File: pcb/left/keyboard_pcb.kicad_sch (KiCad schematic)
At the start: 33 parts, among them J1 TRRS, K00 KEYSW, K01 KEYSW, K02 KEYSW, K03 KEYSW, K04 KEYSW, K05 KEYSW, K10 KEYSW, K11 KEYSW, K12 KEYSW, K13 KEYSW, K14 KEYSW, K15 KEYSW, K20 KEYSW, K21 KEYSW, K22 KEYSW, K23 KEYSW, K24 KEYSW, K25 KEYSW, K30 KEYSW, K31 KEYSW, K32 KEYSW, U2 Pico

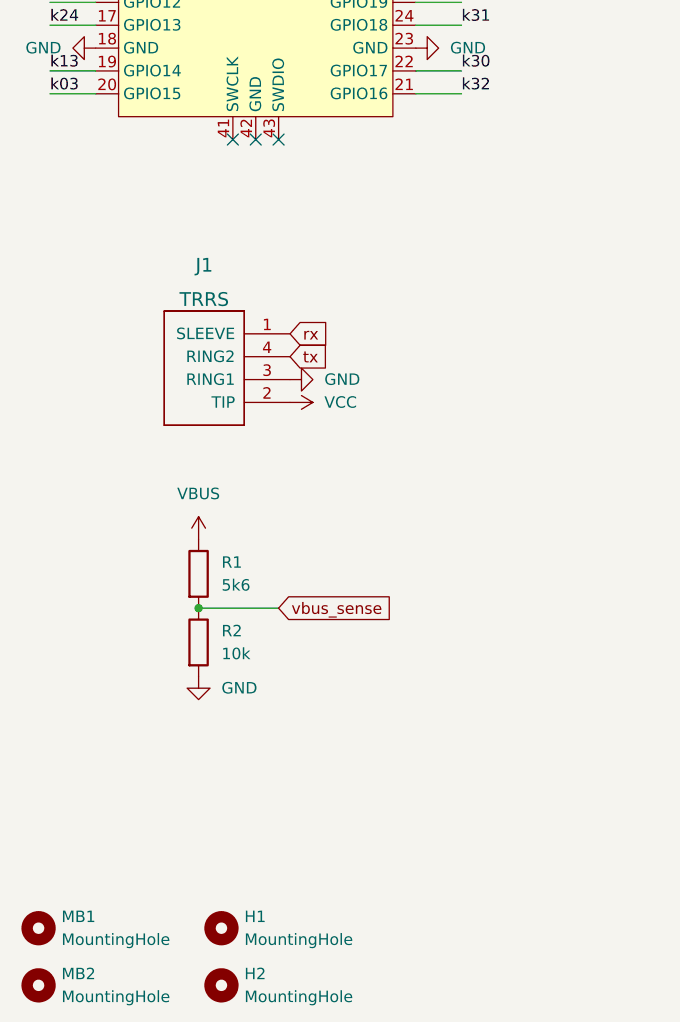
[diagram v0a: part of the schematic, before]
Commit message: Replace TRRS with USB-C on left side
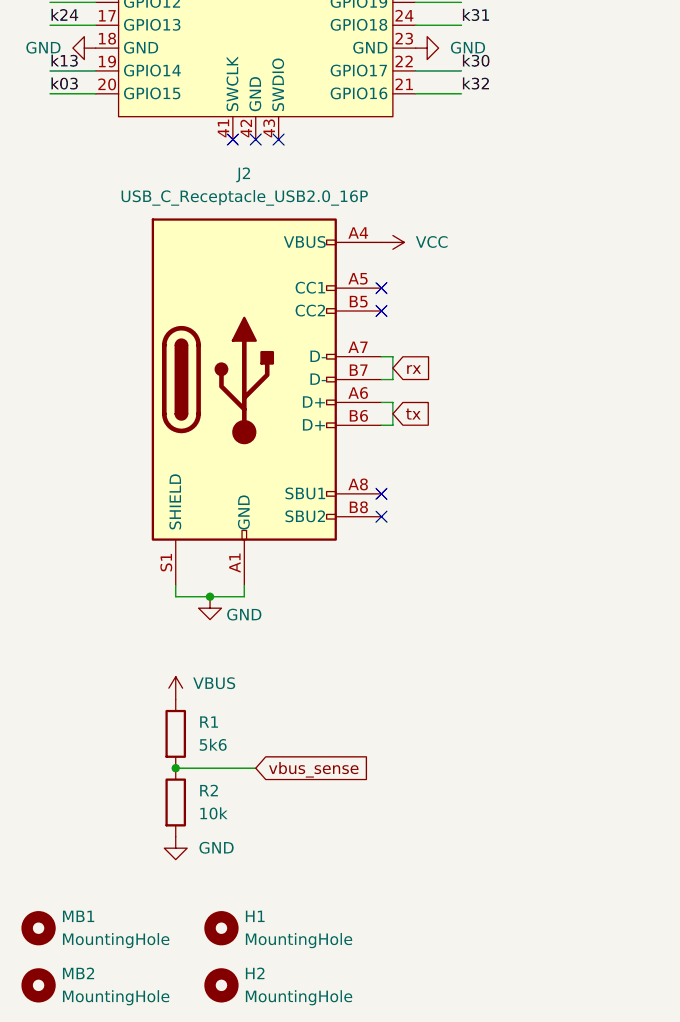
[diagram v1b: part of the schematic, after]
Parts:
- removed J1: TRRS, Resistor_SMD:R_1206_3216Metric_Pad1.30x1.75mm_HandSolder, symbol keebio:TRRS
- added J2: USB_C_Receptacle_USB2.0_16P, Connector_USB:USB_C_Receptacle_Palconn_UTC16-G, symbol Connector:USB_C_Receptacle_USB2.0_16P
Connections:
- net GND: now also J2.A1 (GND), J2.A12 (GND), J2.B1 (GND), J2.B12 (GND), J2.S1 (SHIELD)
- net VCC: now also J2.A4 (VBUS), J2.A9 (VBUS), J2.B4 (VBUS), J2.B9 (VBUS)
- net rx: now also J2.A7 (D-), J2.B7 (D-)
- net tx: now also J2.A6 (D+), J2.B6 (D+)
- no-connect marks 9 -> 13
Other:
- moved on the sheet: R1, R2
